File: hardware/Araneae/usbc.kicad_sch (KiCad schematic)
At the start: 6 parts, among them P1 USB_C_Plug_USB2.0, U11 TPS2041B

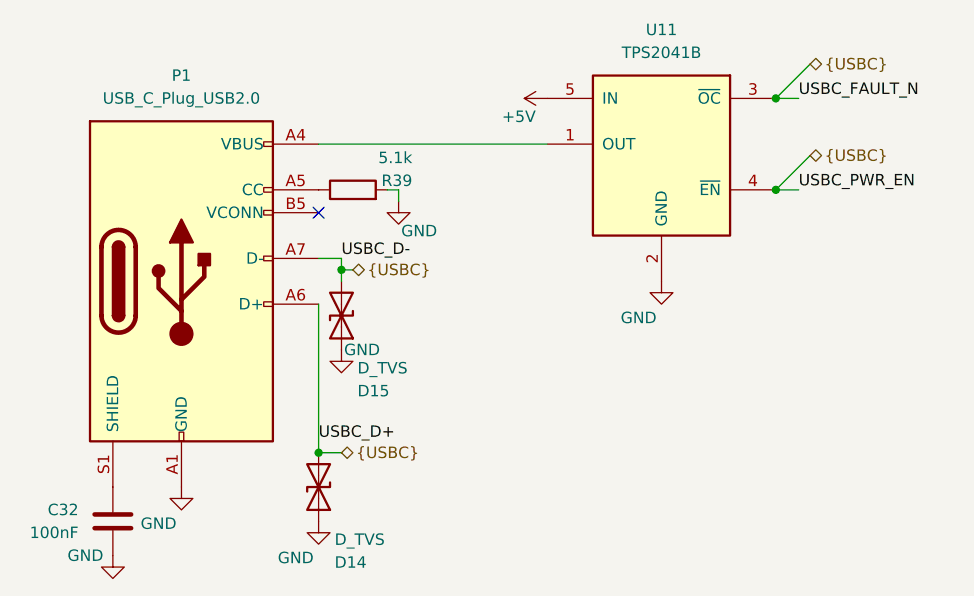
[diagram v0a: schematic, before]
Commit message: Add CI workflow for PCB checks and artifact generation
- Created a GitHub Actions workflow (`ci.yml`) to automate hardware checks including ERC, DRC, and plot generation for KiCad projects.
- Added a new footprint for the SON50P200X200X80-9N component in `SON50P200X200X80-9N.kicad_mod`.
- Introduced a new symbol for the TPS22965DSGR component in `TPS22965DSGR.kicad_sym`.
- Added a configuration file `kibot.yaml` for generating fabrication files and other outputs.
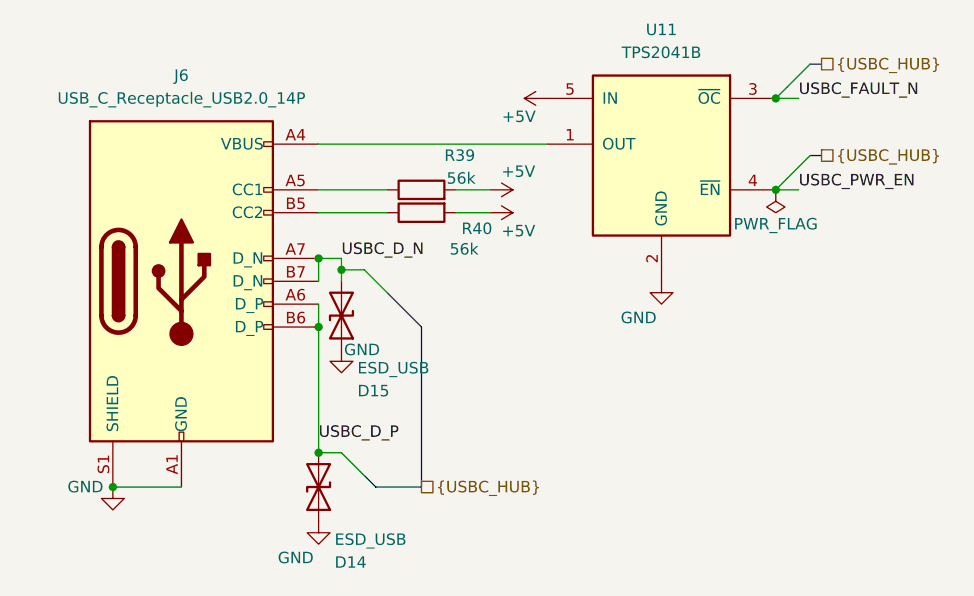
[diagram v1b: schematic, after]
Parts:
- removed C32: 100nF, symbol Device:C
- removed P1: USB_C_Plug_USB2.0, symbol Connector:USB_C_Plug_USB2.0
- added J6: USB_C_Receptacle_USB2.0_14P, Connector_USB:USB_C_Receptacle_HRO_TYPE-C-31-M-12, symbol Connector:USB_C_Receptacle_USB2.0_14P
- added R40: 56k, Resistor_SMD:R_0603_1608Metric, symbol Device:R
- D14, D15: value D_TVS -> ESD_USB; footprint (none) -> Diode_SMD:D_SOD-323
- R39: value 5.1k -> 56k; footprint (none) -> Resistor_SMD:R_0603_1608Metric
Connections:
- net +5V: now also R39.2, R40.2
- net GND: now also J6.A1 (GND), J6.A12 (GND), J6.B1 (GND), J6.B12 (GND), J6.S1 (SHIELD); no longer R39.2
- net at U11.1 (OUT): now also J6.A4 (VBUS), J6.A9 (VBUS), J6.B4 (VBUS), J6.B9 (VBUS)
- net at R39.1: now also J6.A5 (CC1)
- removed net {USBC}: D14.2 (A2), D15.2 (A2), U11.3 (~{OC}), U11.4 (~{EN})
- new net: J6.B5 (CC2), R40.1
- new net USBC_D_N: D15.2 (A2), J6.A7 (D_N), J6.B7 (D_N)
- new net USBC_D_P: D14.2 (A2), J6.A6 (D_P), J6.B6 (D_P)
- new net USBC_FAULT_N: U11.3 (~{OC})
- new net USBC_PWR_EN: U11.4 (~{EN})
- no-connect marks 1 -> 0
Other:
- company: (none) -> Matheus Henrique(Aka: TheusHen)
- title: (none) -> Araneae
- moved on the sheet: R39
